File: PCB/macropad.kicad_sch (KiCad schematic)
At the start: 33 parts, among them SW1 SW_Push, SW10 SW_Push, SW11 SW_Push, SW12 SW_Push, SW13 SW_Push, SW14 SW_Push, SW15 SW_Push, SW16 SW_Push, SW2 SW_Push, SW3 SW_Push, SW4 SW_Push, SW5 SW_Push, SW6 SW_Push, SW7 SW_Push, SW8 SW_Push, SW9 SW_Push, U1 Seeed Studio XIAO SAMD21

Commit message: Finish first state of PCB
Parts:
- removed U1: Seeed Studio XIAO SAMD21, seed:XIAO-SAMD21-RP2040-14P-2.54-21X17.8MM (Seeeduino XIAO), symbol seed:Seeed Studio XIAO SAMD21
- added U2: MOUDLE-SEEEDUINO-XIAO, seed:XIAO-SAMD21-RP2040-14P-2.54-21X17.8MM (Seeeduino XIAO), symbol seed-real:MOUDLE-SEEEDUINO-XIAO
- D1, D10, D11, D12, D13, D14, D15, D16, D2, D3, D4, D5, D6, D7, D8, D9: footprint Diode_THT:D_5KP_P10.16mm_Horizontal -> Diode_THT:D_DO-35_SOD27_P7.62mm_Horizontal
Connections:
- net +3V3: now also U2.12 (3V3)
- net +5V: now also U2.14 (5V)
- net COL0: now also U2.4 (PA11_A3_D3)
- net COL1: now also U2.5 (PA8_A4_D4_SDA)
- net COL2: now also U2.10 (PA5_A9_D9_MISO)
- net COL3: now also U2.11 (PA6_A10_D10_MOSI)
- net GND: now also U2.13 (GND)
- net ROW0: now also U2.6 (PA9_A5_D5_SCL)
- net ROW1: now also U2.7 (PB08_A6_D6_TX)
- net ROW2: now also U2.8 (PB09_A7_D7_RX)
- net ROW3: now also U2.9 (PA7_A8_D8_SCK)

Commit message: LCD!
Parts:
- added Brd1: SSD1306, screen:128x64OLED, symbol screen:SSD1306
- added H1: MountingHole_Pad, Connector_Wire:SolderWire-0.1sqmm_1x01_D0.4mm_OD1mm, symbol Mechanical:MountingHole_Pad
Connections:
- net +5V: now also Brd1.2 (VCC)
- net COL0: now also U2.11 (PA6_A10_D10_MOSI); no longer U2.4 (PA11_A3_D3)
- net COL1: now also U2.10 (PA5_A9_D9_MISO); no longer U2.5 (PA8_A4_D4_SDA)
- net COL2: now also U2.9 (PA7_A8_D8_SCK); no longer U2.10 (PA5_A9_D9_MISO)
- net COL3: now also U2.8 (PB09_A7_D7_RX); no longer U2.11 (PA6_A10_D10_MOSI)
- net GND: now also Brd1.1 (GND)
- net ROW0: now also U2.2 (PA4_A1_D1); no longer U2.6 (PA9_A5_D5_SCL)
- net ROW2: now also U2.4 (PA11_A3_D3); no longer U2.8 (PB09_A7_D7_RX)
- net ROW3: now also U2.3 (PA10_A2_D2); no longer U2.9 (PA7_A8_D8_SCK)
- net at U2.1 (PA02_A0_D0): now also H1.1
- new net: Brd1.4 (SDA), U2.5 (PA8_A4_D4_SDA)
- new net: Brd1.3 (SCL), U2.6 (PA9_A5_D5_SCL)
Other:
- moved on the sheet: U2

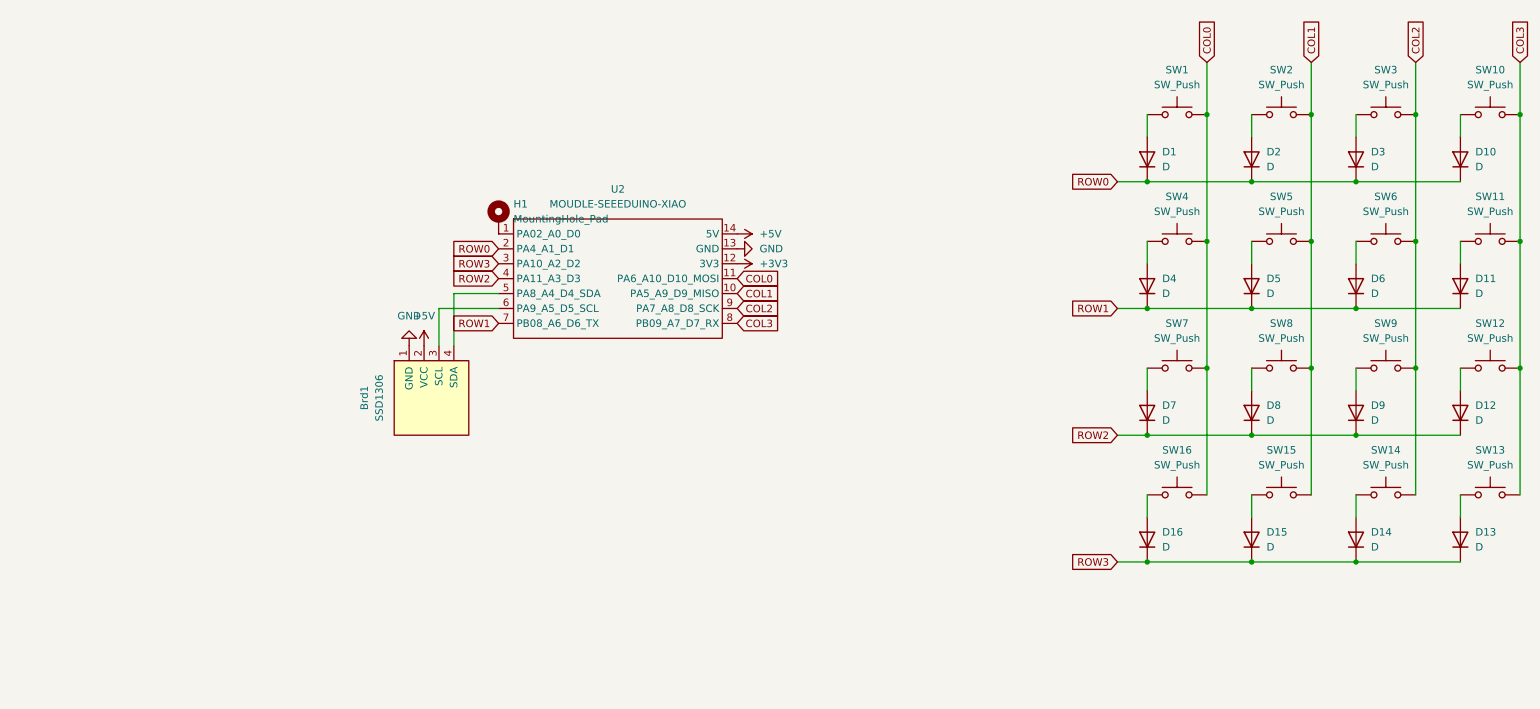
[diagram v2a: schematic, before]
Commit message: Add file names, clean up designators & Improve output
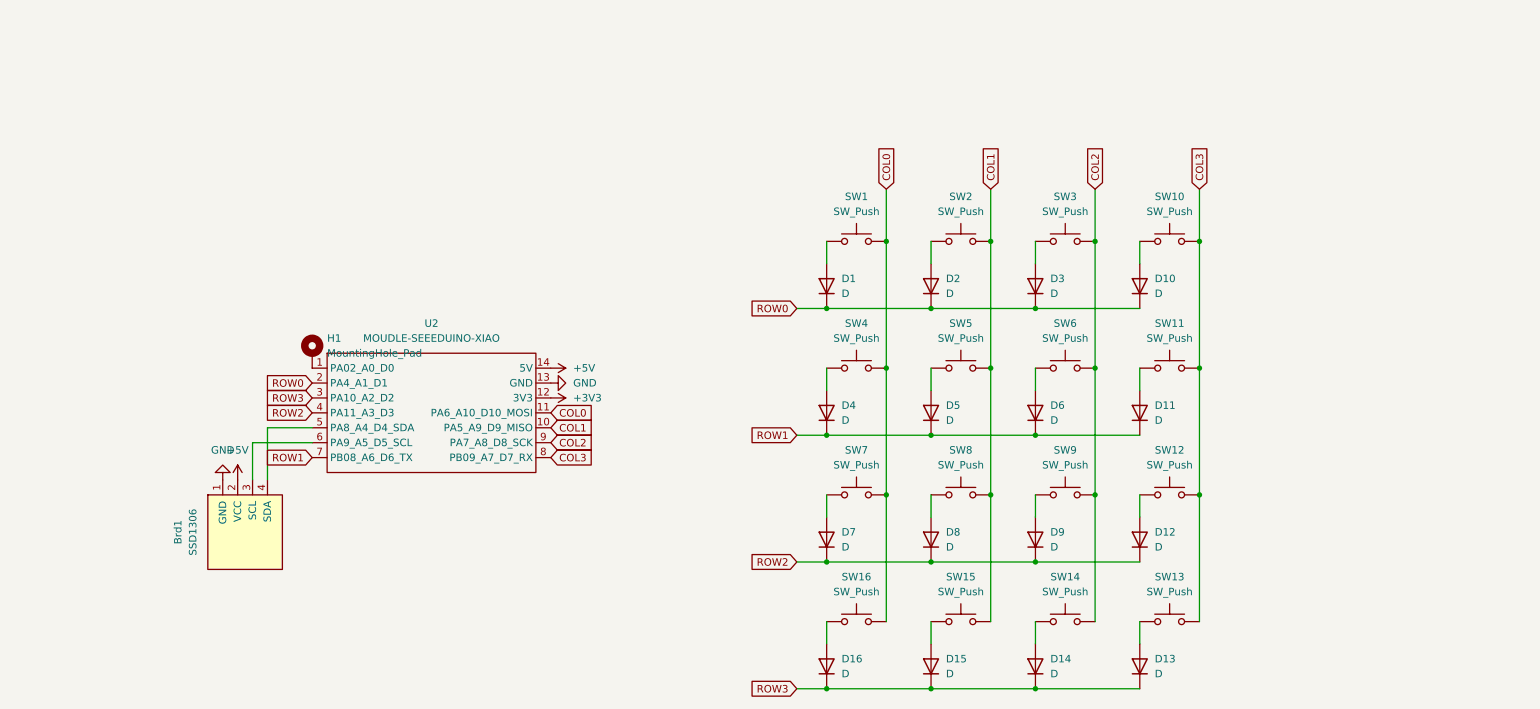
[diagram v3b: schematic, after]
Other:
- company: (none) -> Cheyao
- title: (none) -> Cyao macropad
- moved on the sheet: Brd1, D1, D10, D11, D12, D13, D14, D15, D16, D2, D3, D4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

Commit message: Fix pads
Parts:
- added H1, H2, H3, H4: MountingHole_Pad, MountingHole:MountingHole_3.2mm_M3_Pad, symbol Mechanical:MountingHole_Pad
- renumbered H1 to H5
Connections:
- net GND: now also H1.1, H2.1, H3.1, H4.1
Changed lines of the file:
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@@
     (title "Cyao macropad")
     (date "2024-09-22")
-    (rev "v2")
+    (rev "v2.2")
     (company "Cheyao")
     (comment 1 "https://github.com/cheyao/macropad")
@@
   (junction (at 158.75 67.31) (diameter 0) (color 0 0 0 0)
   )
+  (junction (at 55.88 96.52) (diameter 0) (color 0 0 0 0)
+  )
   (junction (at 186.69 55.88) (diameter 0) (color 0 0 0 0)
   )
@@
   (junction (at 158.75 88.9) (diameter 0) (color 0 0 0 0)
   )
+  (junction (at 43.18 96.52) (diameter 0) (color 0 0 0 0)
+  )
   (junction (at 176.53 88.9) (diameter 0) (color 0 0 0 0)
   )
+  (junction (at 43.18 76.2) (diameter 0) (color 0 0 0 0)
+  )
   (junction (at 222.25 55.88) (diameter 0) (color 0 0 0 0)
   )
@@
   (junction (at 194.31 110.49) (diameter 0) (color 0 0 0 0)
   )
+  (junction (at 43.18 86.36) (diameter 0) (color 0 0 0 0)
+  )
   (junction (at 204.47 77.47) (diameter 0) (color 0 0 0 0)
   )
@@
     (stroke (width 0) (type default))
   )
+  (wire (pts (xy 43.18 86.36) (xy 43.18 96.52))
+    (stroke (width 0) (type default))
+  )
   (wire (pts (xy 176.53 99.06) (xy 176.53 102.87))
     (stroke (width 0) (type default))
@@
     (stroke (width 0) (type default))
   )
+  (wire (pts (xy 43.18 76.2) (xy 43.18 86.36))
+    (stroke (width 0) (type default))
+  )
   (wire (pts (xy 194.31 99.06) (xy 194.31 102.87))
     (stroke (width 0) (type default))
@@
     (stroke (width 0) (type default))
   )
+  (wire (pts (xy 43.18 96.52) (xy 55.88 96.52))
+    (stroke (width 0) (type default))
+  )
   (wire (pts (xy 153.67 67.31) (xy 158.75 67.31))
     (stroke (width 0) (type default))
@@
   )
   (wire (pts (xy 63.5 87.63) (xy 71.12 87.63))
+    (stroke (width 0) (type default))
+  )
+  (wire (pts (xy 43.18 66.04) (xy 43.18 76.2))
     (stroke (width 0) (type default))
   )
@@
     )
   )
+  (symbol (lib_id "Mechanical:MountingHole_Pad") (at 40.64 66.04 90) (unit 1)
+    (in_bom yes) (on_board yes) (dnp no) (fields_autoplaced)
+    (property "Reference" "H4" (at 39.37 59.69 90)
+      (effects (font (size 1.27 1.27)))
+    )
+    (property "Value" "MountingHole_Pad" (at 39.37 62.23 90)
+      (effects (font (size 1.27 1.27)))
+    )
+    (property "Footprint" "MountingHole:MountingHole_3.2mm_M3_Pad" (at 40.64 66.04 0)
+      (effects (font (size 1.27 1.27)) hide)
+    )
+    (property "Datasheet" "~" (at 40.64 66.04 0)
+      (effects (font (size 1.27 1.27)) hide)
+    )
+    (pin "1")
+    (instances
+      (project "macropad"
+        (path "/bbfb2475-963d-4c49-ac81-fadef0dd23d7"
+          (reference "H4") (unit 1)
+        )
+      )
+    )
+  )
   (symbol (lib_id "Device:D") (at 158.75 85.09 90) (unit 1)
     (in_bom yes) (on_board yes) (dnp no) (fields_autoplaced)
@@
         (path "/bbfb2475-963d-4c49-ac81-fadef0dd23d7"
           (reference "D1") (unit 1)
+        )
+      )
+    )
+  )
+  (symbol (lib_id "Mechanical:MountingHole_Pad") (at 40.64 86.36 90) (unit 1)
+    (in_bom yes) (on_board yes) (dnp no) (fields_autoplaced)
+    (property "Reference" "H2" (at 39.37 80.01 90)
+      (effects (font (size 1.27 1.27)))
+    )
+    (property "Value" "MountingHole_Pad" (at 39.37 82.55 90)
+      (effects (font (size 1.27 1.27)))
+    )
+    (property "Footprint" "MountingHole:MountingHole_3.2mm_M3_Pad" (at 40.64 86.36 0)
+      (effects (font (size 1.27 1.27)) hide)
+    )
+    (property "Datasheet" "~" (at 40.64 86.36 0)
+      (effects (font (size 1.27 1.27)) hide)
+    )
+    (pin "1")
+    (instances
+      (project "macropad"
+        (path "/bbfb2475-963d-4c49-ac81-fadef0dd23d7"
+          (reference "H2") (unit 1)
         )
       )
@@
   (symbol (lib_id "Mechanical:MountingHole_Pad") (at 71.12 74.93 0) (unit 1)
     (in_bom yes) (on_board yes) (dnp no) (fields_autoplaced)
-    (property "Reference" "H1" (at 73.66 72.39 0)
+    (property "Reference" "H5" (at 73.66 72.39 0)
       (effects (font (size 1.27 1.27)) (justify left))
     )
@@
       (project "macropad"
         (path "/bbfb2475-963d-4c49-ac81-fadef0dd23d7"
-          (reference "H1") (unit 1)
+          (reference "H5") (unit 1)
         )
       )
@@
         )
       )
+    )
+  )
+  (symbol (lib_id "Mechanical:MountingHole_Pad") (at 40.64 76.2 90) (unit 1)
+    (in_bom yes) (on_board yes) (dnp no) (fields_autoplaced)
+    (property "Reference" "H3" (at 39.37 69.85 90)
+      (effects (font (size 1.27 1.27)))
+    )
+    (property "Value" "MountingHole_Pad" (at 39.37 72.39 90)
+      (effects (font (size 1.27 1.27)))
+    )
+    (property "Footprint" "MountingHole:MountingHole_3.2mm_M3_Pad" (at 40.64 76.2 0)
+      (effects (font (size 1.27 1.27)) hide)
+    )
+    (property "Datasheet" "~" (at 40.64 76.2 0)
+      (effects (font (size 1.27 1.27)) hide)
+    )
+    (pin "1")
+    (instances
+      (project "macropad"
+        (path "/bbfb2475-963d-4c49-ac81-fadef0dd23d7"
+          (reference "H3") (unit 1)
+        )
+      )
+    )
+  )
+  (symbol (lib_id "Mechanical:MountingHole_Pad") (at 40.64 96.52 90) (unit 1)
+    (in_bom yes) (on_board yes) (dnp no) (fields_autoplaced)
+    (property "Reference" "H1" (at 39.37 90.17 90)
+      (effects (font (size 1.27 1.27)))
+    )
+    (property "Value" "MountingHole_Pad" (at 39.37 92.71 90)
+      (effects (font (size 1.27 1.27)))
+    )
+    (property "Footprint" "MountingHole:MountingHole_3.2mm_M3_Pad" (at 40.64 96.52 0)
+      (effects (font (size 1.27 1.27)) hide)
+    )
+    (property "Datasheet" "~" (at 40.64 96.52 0)
+      (effects (font (size 1.27 1.27)) hide)
+    )
+    (pin "1")
+    (instances
+      (project "macropad"
+        (path "/bbfb2475-963d-4c49-ac81-fadef0dd23d7"
+          (reference "H1") (unit 1)
+        )
+      )
